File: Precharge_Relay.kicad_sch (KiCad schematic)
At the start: 7 parts, among them K3 G2RL-1A, Q7 DMN61D8LQ, Q8 DMN61D8LQ

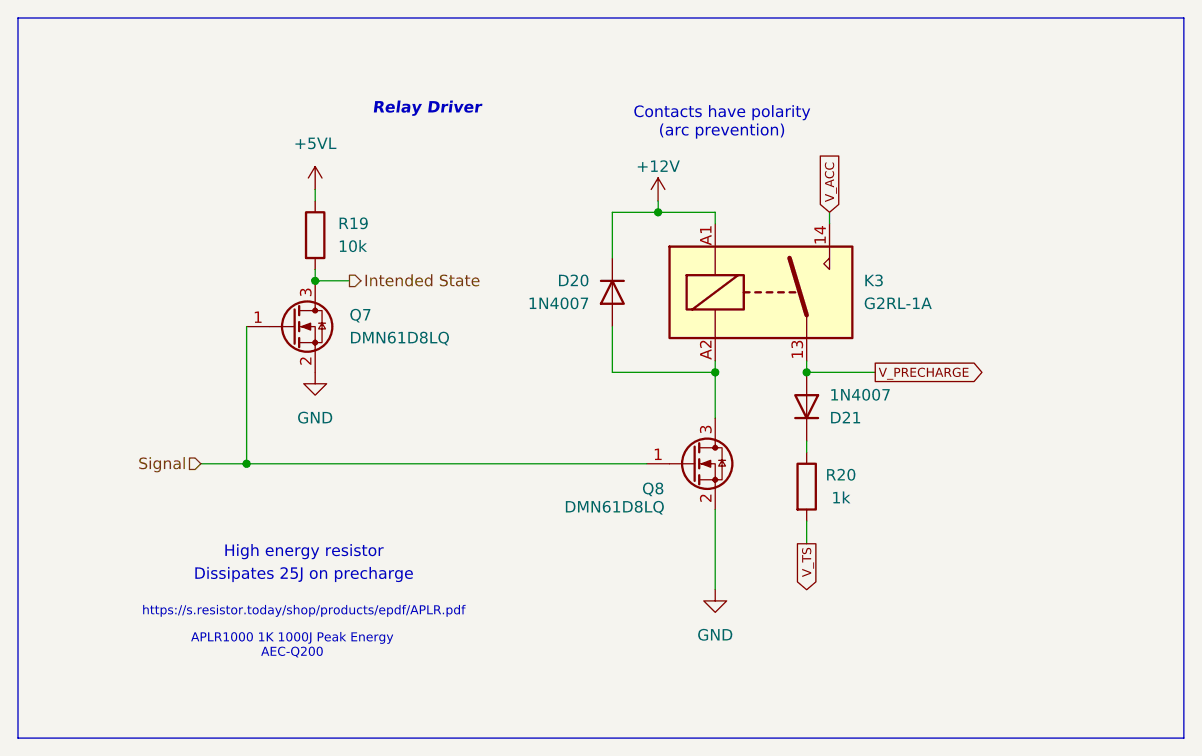
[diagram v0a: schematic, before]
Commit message: schematic: Assign all footprints
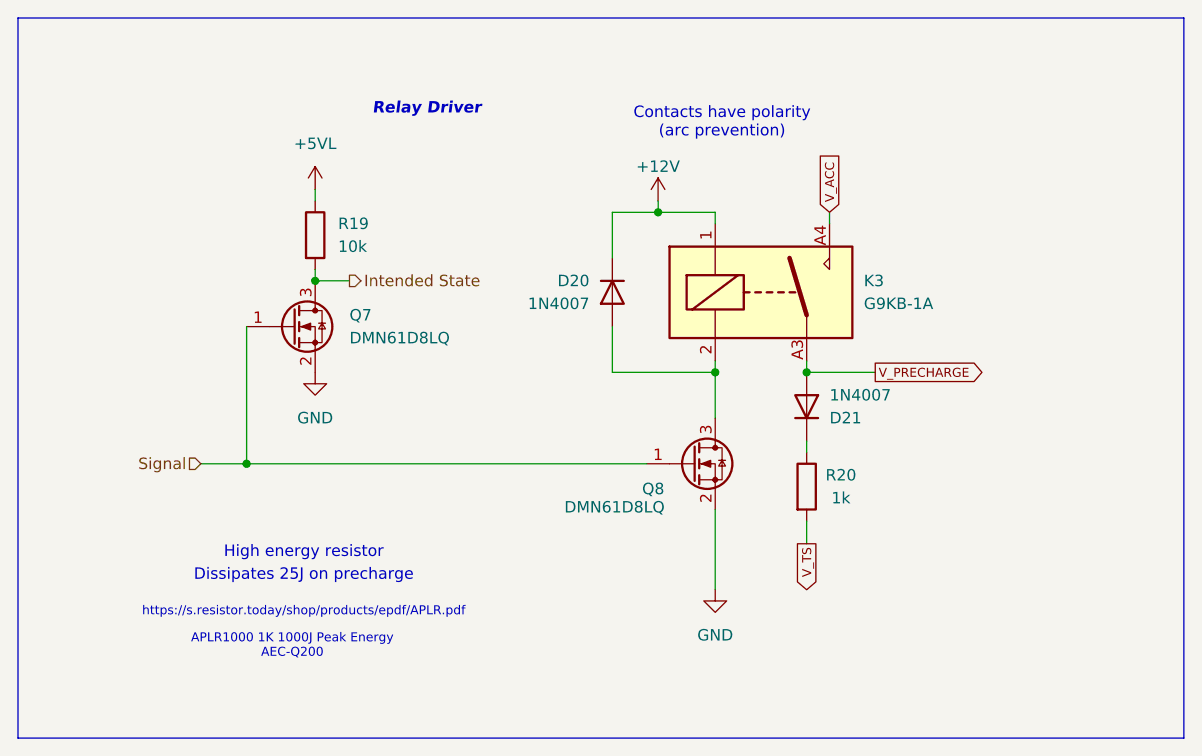
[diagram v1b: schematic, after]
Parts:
- removed K3: G2RL-1A, Relay_THT:Relay_SPST_Omron_G2RL-1A, symbol Relay:G2RL-1A
- added K3: G9KB-1A, yfs:G9KB-1A, symbol yfs:G9KB-1A
- R20: footprint Resistor_SMD:R_0603_1608Metric -> yfs:APLR1000
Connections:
- net +12V: now also K3.1
- net V_ACC: now also K3.A4, K3.B4
- net V_PRECHARGE: now also K3.A3, K3.B3
- net at D20.2 (A), Q8.3 (D): now also K3.2
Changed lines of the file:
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@@
 			)
 		)
-		(property "Footprint" "Resistor_SMD:R_0603_1608Metric"
+		(property "Footprint" "yfs:APLR1000"
 			(at 118.872 86.36 90)
 			(effects
@@
 	)
 	(symbol
-		(lib_id "Relay:G2RL-1A")
+		(lib_id "yfs:G9KB-1A")
 		(at 115.57 64.77 0)
 		(unit 1)
@@
 			)
 		)
-		(property "Value" "G2RL-1A"
+		(property "Value" "G9KB-1A"
 			(at 127 66.0399 0)
 			(effects
@@
 			)
 		)
-		(property "Footprint" "Relay_THT:Relay_SPST_Omron_G2RL-1A"
-			(at 127 66.04 0)
-			(effects
-				(font
-					(size 1.27 1.27)
-				)
-				(justify left)
-				(hide yes)
-			)
-		)
-		(property "Datasheet" "https://omronfs.omron.com/en_US/ecb/products/pdf/en-g2rl.pdf"
-			(at 115.57 64.77 0)
-			(effects
-				(font
-					(size 1.27 1.27)
-				)
-				(hide yes)
-			)
-		)
-		(property "Description" "General Purpose Low Profile Relay SPST Through Hole, Omron G2RL series, Normally Open, 12A 250VAC"
-			(at 115.57 64.77 0)
-			(effects
-				(font
-					(size 1.27 1.27)
-				)
-				(hide yes)
-			)
-		)
-		(pin "13"
-		)
-		(pin "14"
-		)
-		(pin "A1"
-		)
-		(pin "A2"
-		)
-		(instances
-			(project "Precharge_PCB"
+		(property "Footprint" "yfs:G9KB-1A"
+			(at 100.33 42.164 0)
+			(effects
+				(font
+					(size 1.27 1.27)
+				)
+				(justify left)
+				(hide yes)
+			)
+		)
+		(property "Datasheet" "https://components.omron.com/us-en/sites/components.omron.com.us/files/datasheet_pdf/K340-E1.pdf"
+			(at 116.332 42.926 0)
+			(effects
+				(font
+					(size 1.27 1.27)
+				)
+				(hide yes)
+			)
+		)
+		(property "Description" "General Purpose Relay SPST-NO (1 Form A) 12VDC Coil Through Hole"
+			(at 114.554 39.37 0)
+			(effects
+				(font
+					(size 1.27 1.27)
+				)
+				(hide yes)
+			)
+		)
+		(pin "B4"
+		)
+		(pin "A4"
+		)
+		(pin "1"
+		)
+		(pin "2"
+		)
+		(pin "A3"
+		)
+		(pin "B3"
+		)
+		(instances
+			(project ""
 				(path "/c467677d-b98c-4488-bd11-965ef67263b2/c2fa71c2-1bd3-4dc0-8faf-814cfbc0b0db"
 					(reference "K3")

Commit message: schematic: Power precharge relay from shutdown
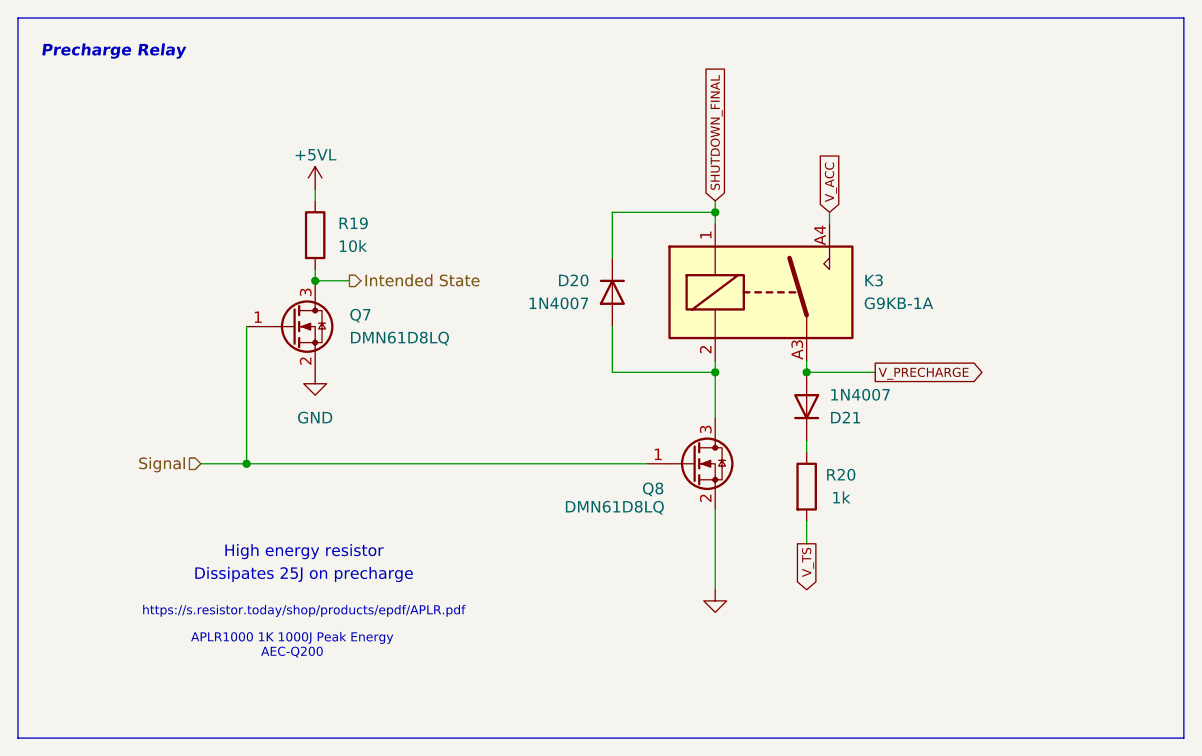
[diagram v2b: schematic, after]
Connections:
- net +12V renamed SHUTDOWN_FINAL
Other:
- note added: "Precharge Relay"
- note removed: "Contacts have polarity (arc prevention)"
- note removed: "Relay Driver"
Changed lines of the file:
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@@
 		)
 	)
-	(text "Relay Driver"
-		(exclude_from_sim no)
-		(at 72.39 44.45 0)
+	(text "Precharge Relay"
+		(exclude_from_sim no)
+		(at 35.56 38.1 0)
 		(effects
 			(font
@@
 		)
 	)
-	(text "Contacts have polarity\n(arc prevention)"
-		(exclude_from_sim no)
-		(at 111.252 45.974 0)
-		(effects
-			(font
-				(size 1.27 1.27)
-			)
-		)
-	)
-	(junction
-		(at 104.14 55.88)
-		(diameter 0)
-		(color 0 0 0 0)
-	)
 	(junction
 		(at 58.42 83.82)
@@
 	)
 	(junction
+		(at 110.49 55.88)
+		(diameter 0)
+		(color 0 0 0 0)
+	)
+	(junction
 		(at 120.65 73.66)
 		(diameter 0)
@@
 	(wire
 		(pts
-			(xy 99.06 55.88) (xy 104.14 55.88)
+			(xy 99.06 55.88) (xy 110.49 55.88)
 		)
 		(stroke
@@
 	(wire
 		(pts
-			(xy 104.14 54.61) (xy 104.14 55.88)
-		)
-		(stroke
-			(width 0)
-			(type default)
-		)
-	)
-	(wire
-		(pts
 			(xy 58.42 68.58) (xy 58.42 83.82)
 		)
@@
 	(wire
 		(pts
+			(xy 110.49 54.61) (xy 110.49 55.88)
+		)
+		(stroke
+			(width 0)
+			(type default)
+		)
+	)
+	(wire
+		(pts
 			(xy 99.06 73.66) (xy 110.49 73.66)
 		)
@@
 	(wire
 		(pts
-			(xy 104.14 55.88) (xy 110.49 55.88)
-		)
-		(stroke
-			(width 0)
-			(type default)
-		)
-	)
-	(wire
-		(pts
 			(xy 120.65 82.55) (xy 120.65 81.28)
 		)
@@
 			(width 0)
 			(type default)
+		)
+	)
+	(global_label "SHUTDOWN_FINAL"
+		(shape input)
+		(at 110.49 54.61 90)
+		(fields_autoplaced yes)
+		(effects
+			(font
+				(size 1 1)
+			)
+			(justify left)
+		)
+		(property "Intersheetrefs" "${INTERSHEET_REFS}"
+			(at 110.49 39.4027 90)
+			(effects
+				(font
+					(size 1.27 1.27)
+				)
+				(justify left)
+				(hide yes)
+			)
 		)
 	)
@@
 		(on_board yes)
 		(dnp no)
-		(fields_autoplaced yes)
 		(property "Reference" "#PWR055"
 			(at 66.04 57.15 0)
@@
 		)
 		(property "Value" "+5VL"
-			(at 66.04 48.26 0)
+			(at 66.04 49.53 0)
 			(effects
 				(font
@@
 				(path "/c467677d-b98c-4488-bd11-965ef67263b2/c2fa71c2-1bd3-4dc0-8faf-814cfbc0b0db"
 					(reference "#PWR055")
-					(unit 1)
-				)
-			)
-		)
-	)
-	(symbol
-		(lib_id "power:+12V")
-		(at 104.14 54.61 0)
-		(unit 1)
-		(exclude_from_sim no)
-		(in_bom yes)
-		(on_board yes)
-		(dnp no)
-		(property "Reference" "#PWR057"
-			(at 104.14 58.42 0)
-			(effects
-				(font
-					(size 1.27 1.27)
-				)
-				(hide yes)
-			)
-		)
-		(property "Value" "+12V"
-			(at 104.14 50.8 0)
-			(effects
-				(font
-					(size 1.27 1.27)
-				)
-			)
-		)
-		(property "Footprint" ""
-			(at 104.14 54.61 0)
-			(effects
-				(font
-					(size 1.27 1.27)
-				)
-				(hide yes)
-			)
-		)
-		(property "Datasheet" ""
-			(at 104.14 54.61 0)
-			(effects
-				(font
-					(size 1.27 1.27)
-				)
-				(hide yes)
-			)
-		)
-		(property "Description" "Power symbol creates a global label with name \"+12V\""
-			(at 104.14 54.61 0)
-			(effects
-				(font
-					(size 1.27 1.27)
-				)
-				(hide yes)
-			)
-		)
-		(pin "1"
-		)
-		(instances
-			(project "Precharge_PCB"
-				(path "/c467677d-b98c-4488-bd11-965ef67263b2/c2fa71c2-1bd3-4dc0-8faf-814cfbc0b0db"
-					(reference "#PWR057")
 					(unit 1)
 				)
@@
 		(on_board yes)
 		(dnp no)
-		(fields_autoplaced yes)
 		(property "Reference" "#PWR058"
 			(at 110.49 104.14 0)
@@
 		)
 		(property "Value" "GND"
-			(at 110.49 102.87 0)
-			(effects
-				(font
-					(size 1.27 1.27)
-				)
-			)
-		)
+			(at 110.49 101.6 0)
+			(effects
+				(font
+					(size 1.27 1.27)
+				)
+				(hide yes)
+			)
+		)

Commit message: schematic: Reassign reference designators
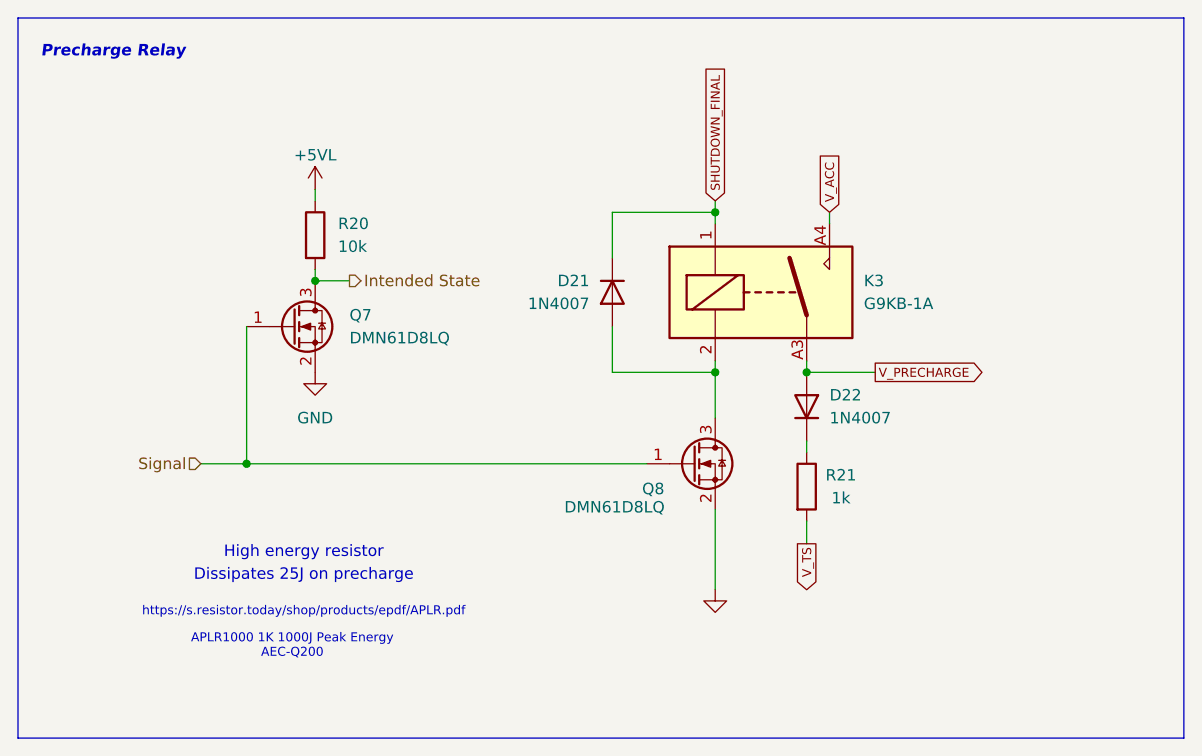
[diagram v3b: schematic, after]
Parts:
- renumbered D20 to D21, D21 to D22, R19 to R20, R20 to R21
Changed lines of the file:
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@@
 		(on_board yes)
 		(dnp no)
-		(property "Reference" "D20"
+		(property "Reference" "D21"
 			(at 96.52 63.4999 90)
 			(effects
@@
 			(project "Precharge_PCB"
 				(path "/c467677d-b98c-4488-bd11-965ef67263b2/c2fa71c2-1bd3-4dc0-8faf-814cfbc0b0db"
-					(reference "D20")
+					(reference "D21")
 					(unit 1)
 				)
@@
 		(on_board yes)
 		(dnp no)
-		(property "Reference" "D21"
-			(at 123.19 78.7401 90)
+		(property "Reference" "D22"
+			(at 123.19 76.2 90)
 			(effects
 				(font
@@
 		)
 		(property "Value" "1N4007"
-			(at 123.19 76.2001 90)
+			(at 123.19 78.74 90)
 			(effects
 				(font
@@
 			(project "Precharge_PCB"
 				(path "/c467677d-b98c-4488-bd11-965ef67263b2/c2fa71c2-1bd3-4dc0-8faf-814cfbc0b0db"
-					(reference "D21")
+					(reference "D22")
 					(unit 1)
 				)
@@
 		(on_board yes)
 		(dnp no)
-		(property "Reference" "R20"
+		(property "Reference" "R21"
 			(at 124.46 85.09 0)
 			(effects
@@
 			(project "Precharge_PCB"
 				(path "/c467677d-b98c-4488-bd11-965ef67263b2/c2fa71c2-1bd3-4dc0-8faf-814cfbc0b0db"
-					(reference "R20")
+					(reference "R21")
 					(unit 1)
 				)
@@
 		(dnp no)
 		(fields_autoplaced yes)
-		(property "Reference" "R19"
+		(property "Reference" "R20"
 			(at 68.58 57.1499 0)
 			(effects
@@
 			(project "Precharge_PCB"
 				(path "/c467677d-b98c-4488-bd11-965ef67263b2/c2fa71c2-1bd3-4dc0-8faf-814cfbc0b0db"
-					(reference "R19")
-					(unit 1)
-				)
+					(reference "R20")
+					(unit 1)
+				)

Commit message: schematic: Fill out most of the BOM
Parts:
- K3: Dist (none) -> Mouser; Dist # (none) -> 653-G9KB-1ADC12; Mfr (none) -> Omron; Mfr # (none) -> G9KB-1ADC12
- Q7, Q8: Dist (none) -> LCSC; Dist # (none) -> C5248874; Mfr (none) -> DIODES; Mfr # (none) -> DMN61D8LQ-7
- R20: Dist (none) -> LCSC; Dist # (none) -> C25804; Mfr (none) -> Uni-Royal; Mfr # (none) -> 0603WAF1002T5E
- R21: Dist (none) -> DigiKey; Dist # (none) -> 4506-APLR1000J1K00SE-ND; Mfr (none) -> C&B/RESI; Mfr # (none) -> APLR1000J1K00SE
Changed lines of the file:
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@@
+			)
+		)
+		(property "Dist" "DigiKey"
+			(at 120.65 86.36 0)
+			(effects
+				(font
+					(size 1.27 1.27)
+				)
+				(hide yes)
+			)
+		)
+		(property "Dist #" "4506-APLR1000J1K00SE-ND"
+			(at 120.65 86.36 0)
+			(effects
+				(font
+					(size 1.27 1.27)
+				)
+				(hide yes)
+			)
+		)
+		(property "Mfr" "C&B/RESI"
+			(at 120.65 86.36 0)
+			(effects
+				(font
+					(size 1.27 1.27)
+				)
+				(hide yes)
+			)
+		)
+		(property "Mfr #" "APLR1000J1K00SE"
+			(at 120.65 86.36 0)
+			(effects
+				(font
+					(size 1.27 1.27)
+				)
+				(hide yes)
 			)
 		)
@@
 		)
 		(property "Description" "60V Vds, 0.470A Id, N-Channel MOSFET for switching inductive loads , SOT-23"
+			(at 107.95 83.82 0)
+			(effects
+				(font
+					(size 1.27 1.27)
+				)
+				(hide yes)
+			)
+		)
+		(property "Dist" "LCSC"
+			(at 107.95 83.82 0)
+			(effects
+				(font
+					(size 1.27 1.27)
+				)
+				(hide yes)
+			)
+		)
+		(property "Dist #" "C5248874"
+			(at 107.95 83.82 0)
+			(effects
+				(font
+					(size 1.27 1.27)
+				)
+				(hide yes)
+			)
+		)
+		(property "Mfr" "DIODES"
+			(at 107.95 83.82 0)
+			(effects
+				(font
+					(size 1.27 1.27)
+				)
+				(hide yes)
+			)
+		)
+		(property "Mfr #" "DMN61D8LQ-7"
 			(at 107.95 83.82 0)
 			(effects
@@
 			)
 		)
+		(property "Dist" "LCSC"
+			(at 66.04 58.42 0)
+			(effects
+				(font
+					(size 1.27 1.27)
+				)
+				(hide yes)
+			)
+		)
+		(property "Dist #" "C25804"
+			(at 66.04 58.42 0)
+			(effects
+				(font
+					(size 1.27 1.27)
+				)
+				(hide yes)
+			)
+		)
+		(property "Mfr" "Uni-Royal"
+			(at 66.04 58.42 0)
+			(effects
+				(font
+					(size 1.27 1.27)
+				)
+				(hide yes)
+			)
+		)
+		(property "Mfr #" "0603WAF1002T5E"
+			(at 66.04 58.42 0)
+			(effects
+				(font
+					(size 1.27 1.27)
+				)
+				(hide yes)
+			)
+		)
 		(pin "1"
 		)
@@
 		)
 		(property "Description" "60V Vds, 0.470A Id, N-Channel MOSFET for switching inductive loads , SOT-23"
+			(at 63.5 68.58 0)
+			(effects
+				(font
+					(size 1.27 1.27)
+				)
+				(hide yes)
+			)
+		)
+		(property "Dist" "LCSC"
+			(at 63.5 68.58 0)
+			(effects
+				(font
+					(size 1.27 1.27)
+				)
+				(hide yes)
+			)
+		)
+		(property "Dist #" "C5248874"
+			(at 63.5 68.58 0)
+			(effects
+				(font
+					(size 1.27 1.27)
+				)
+				(hide yes)
+			)
+		)
+		(property "Mfr" "DIODES"
+			(at 63.5 68.58 0)
+			(effects
+				(font
+					(size 1.27 1.27)
+				)
+				(hide yes)
+			)
+		)
+		(property "Mfr #" "DMN61D8LQ-7"
 			(at 63.5 68.58 0)
 			(effects
@@
 			(effects
 				(font
+					(size 1.27 1.27)
+				)
+				(hide yes)
+			)
+		)
+		(property "Dist" "Mouser"
+			(at 115.57 64.77 0)
+			(effects
+				(font
+					(size 1.27 1.27)
+				)
+				(hide yes)
+			)
+		)
+		(property "Dist #" "653-G9KB-1ADC12"
+			(at 115.57 64.77 0)
+			(effects
+				(font
+					(size 1.27 1.27)
+				)
+				(hide yes)
+			)
+		)
+		(property "Mfr" "Omron"
+			(at 115.57 64.77 0)
+			(effects
+				(font
+					(size 1.27 1.27)
+				)
+				(hide yes)
+			)
+		)
+		(property "Mfr #" "G9KB-1ADC12"
+			(at 115.57 64.77 0)
+			(effects
+				(font

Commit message: Revision A
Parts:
- removed K3: G9KB-1A, yfs:G9KB-1A, symbol yfs:G9KB-1A
- added K3: G9EJH-1-E, yfs:G9EJH-1-E, symbol yfs:G9EJH-1-E
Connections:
- net SHUTDOWN_FINAL: now also K3.1
- net V_ACC: now also K3.A4, K3.B4
- net V_PRECHARGE: now also K3.A3, K3.B3
- net at D21.2 (A), Q8.3 (D): now also K3.2
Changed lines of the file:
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@@
+	)
+	(symbol
+		(lib_id "yfs:G9EJH-1-E")
+		(at 115.57 64.77 0)
+		(unit 1)
+		(exclude_from_sim no)
+		(in_bom yes)
+		(on_board yes)
+		(dnp no)
+		(fields_autoplaced yes)
+		(property "Reference" "K3"
+			(at 127 63.4999 0)
+			(effects
+				(font
+					(size 1.27 1.27)
+				)
+				(justify left)
+			)
+		)
+		(property "Value" "G9EJH-1-E"
+			(at 127 66.0399 0)
+			(effects
+				(font
+					(size 1.27 1.27)
+				)
+				(justify left)
+			)
+		)
+		(property "Footprint" "yfs:G9EJH-1-E"
+			(at 115.57 64.77 0)
+			(effects
+				(font
+					(size 1.27 1.27)
+				)
+				(hide yes)
+			)
+		)
+		(property "Datasheet" "https://www.mouser.com/catalog/specsheets/Omron_07-02-2025_G9EJH-1-E_Datasheet.pdf"
+			(at 111.506 47.244 0)
+			(effects
+				(font
+					(size 1.27 1.27)
+				)
+				(hide yes)
+			)
+		)
+		(property "Description" "Small size DC power relay for 800 VDC systems specialized for pre-charging applications"
+			(at 111.506 47.244 0)
+			(effects
+				(font
+					(size 1.27 1.27)
+				)
+				(hide yes)
+			)
+		)
+		(pin "A4"
+		)
+		(pin "B3"
+		)
+		(pin "1"
+		)
+		(pin "A3"
+		)
+		(pin "2"
+		)
+		(pin "B4"
+		)
+		(instances
+			(project ""
+				(path "/c467677d-b98c-4488-bd11-965ef67263b2/c2fa71c2-1bd3-4dc0-8faf-814cfbc0b0db"
+					(reference "K3")
+					(unit 1)
+				)
+			)
+		)
 	)
 	(symbol
@@
 					(unit 1)
 				)
-			)
-		)
-	)
-	(symbol
-		(lib_id "yfs:G9KB-1A")
-		(at 115.57 64.77 0)
-		(unit 1)
-		(exclude_from_sim no)
-		(in_bom yes)
-		(on_board yes)
-		(dnp no)
-		(fields_autoplaced yes)
-		(property "Reference" "K3"
-			(at 127 63.4999 0)
-			(effects
-				(font
-					(size 1.27 1.27)
-				)
-				(justify left)
-			)
-		)
-		(property "Value" "G9KB-1A"
-			(at 127 66.0399 0)
-			(effects
-				(font
-					(size 1.27 1.27)
-				)
-				(justify left)
-			)
-		)
-		(property "Footprint" "yfs:G9KB-1A"
-			(at 100.33 42.164 0)
-			(effects
-				(font
-					(size 1.27 1.27)
-				)
-				(justify left)
-				(hide yes)
-			)
-		)
-		(property "Datasheet" "https://components.omron.com/us-en/sites/components.omron.com.us/files/datasheet_pdf/K340-E1.pdf"
-			(at 116.332 42.926 0)
-			(effects
-				(font
-					(size 1.27 1.27)
-				)
-				(hide yes)
-			)
-		)
-		(property "Description" "General Purpose Relay SPST-NO (1 Form A) 12VDC Coil Through Hole"
-			(at 114.554 39.37 0)
-			(effects
-				(font
-					(size 1.27 1.27)
-				)
-				(hide yes)
-			)
-		)
-		(property "Dist" "Mouser"
-			(at 115.57 64.77 0)
-			(effects
-				(font
-					(size 1.27 1.27)
-				)
-				(hide yes)
-			)
-		)
-		(property "Dist #" "653-G9KB-1ADC12"
-			(at 115.57 64.77 0)
-			(effects
-				(font
-					(size 1.27 1.27)
-				)
-				(hide yes)
-			)
-		)
-		(property "Mfr" "Omron"
-			(at 115.57 64.77 0)
-			(effects
-				(font
-					(size 1.27 1.27)
-				)
-				(hide yes)
-			)
-		)
-		(property "Mfr #" "G9KB-1ADC12"
-			(at 115.57 64.77 0)
-			(effects
-				(font
-					(size 1.27 1.27)
-				)
-				(hide yes)
-			)
-		)
-		(pin "B4"
-		)
-		(pin "A4"
-		)
-		(pin "1"
-		)
-		(pin "2"
-		)
-		(pin "A3"
-		)
-		(pin "B3"
-		)
-		(instances
-			(project ""
-				(path "/c467677d-b98c-4488-bd11-965ef67263b2/c2fa71c2-1bd3-4dc0-8faf-814cfbc0b0db"
-					(reference "K3")
-					(unit 1)
-				)
